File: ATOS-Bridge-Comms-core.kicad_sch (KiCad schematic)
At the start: 61 parts, among them J2 Conn_02x05_Counter_Clockwise, J3 Conn_01x09_Pin, Q1 2SC4617R, Q3 UMH3N, SW2 SKRPACE010, SW3 SKRPACE010, U1 LAN8720A-CP-TR, U2 AMS1117-3.3, U3 CH340C, U4 ESP32-WROOM-32UE, X1 ECS-2520MV-250-CN-TR

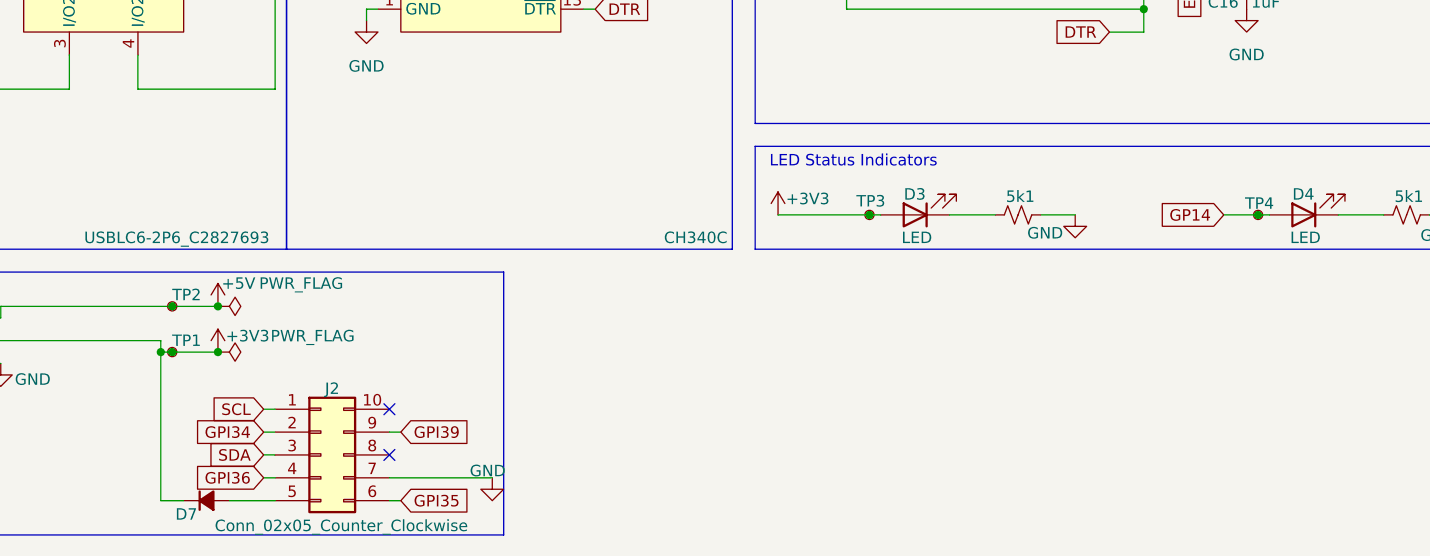
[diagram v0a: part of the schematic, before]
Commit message: Swap AMS1117-3.3 to LCSC C347222, add fab outputs
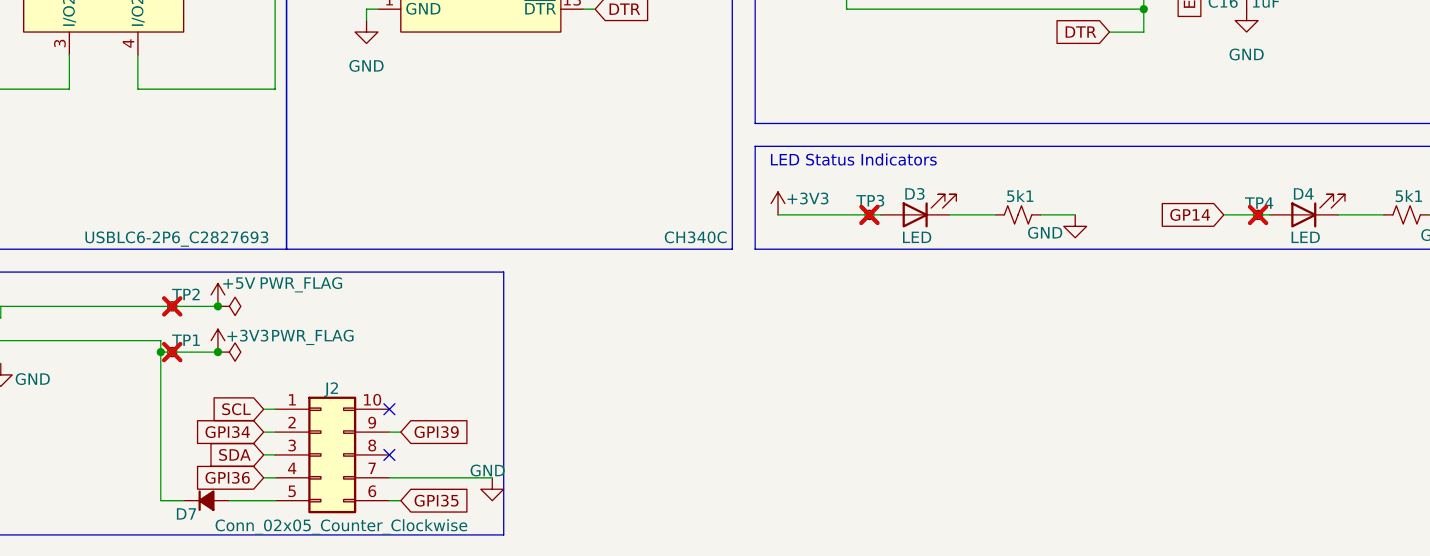
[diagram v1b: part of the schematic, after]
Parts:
- C1, C4, C5, C7, C9: LCSC Part (none) -> C19711
- C10: LCSC Part (none) -> C1556
- C12, C14, C2, C3, C6, C8: LCSC Part (none) -> C1525
- C15: LCSC Part (none) -> C86295
- C16: LCSC Part (none) -> C52923
- TP1, TP2, TP3, TP4: now not fitted
- U2: LCSC Part (none) -> C6186
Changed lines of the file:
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@@
 			)
 		)
+		(property "LCSC Part" "C6186"
+			(at 33.02 170.18 0)
+			(hide yes)
+			(show_name no)
+			(do_not_autoplace no)
+			(effects
+				(font
+					(size 1.27 1.27)
+				)
+			)
+		)
 		(pin "1"
 		)
@@
 			)
 		)
+		(property "LCSC Part" "C1525"
+			(at 102.87 118.11 90)
+			(hide yes)
+			(show_name no)
+			(do_not_autoplace no)
+			(effects
+				(font
+					(size 1.27 1.27)
+				)
+			)
+		)
 		(pin "2"
 		)
@@
 		(on_board yes)
 		(in_pos_files yes)
-		(dnp no)
+		(dnp yes)
 		(property "Reference" "TP4"
 			(at 259.588 158.75 90)
@@
 			)
 		)
+		(property "LCSC Part" "C1525"
+			(at 24.13 120.65 0)
+			(hide yes)
+			(show_name no)
+			(do_not_autoplace no)
+			(effects
+				(font
+					(size 1.27 1.27)
+				)
+			)
+		)
 		(pin "2"
 		)
@@
 			)
 		)
+		(property "LCSC Part" "C1525"
+			(at 88.9 29.21 0)
+			(hide yes)
+			(show_name no)
+			(do_not_autoplace no)
+			(effects
+				(font
+					(size 1.27 1.27)
+				)
+			)
+		)
 		(pin "2"
 		)
@@
 			)
 		)
+		(property "LCSC Part" "C1556"
+			(at 146.05 78.74 0)
+			(hide yes)
+			(show_name no)
+			(do_not_autoplace no)
+			(effects
+				(font
+					(size 1.27 1.27)
+				)
+			)
+		)
 		(pin "2"
 		)
@@
 			)
 		)
+		(property "LCSC Part" "C19711"
+			(at 100.33 29.21 0)
+			(hide yes)
+			(show_name no)
+			(do_not_autoplace no)
+			(effects
+				(font
+					(size 1.27 1.27)
+				)
+			)
+		)
 		(pin "2"
 		)
@@
 		(on_board yes)
 		(in_pos_files yes)
-		(dnp no)
+		(dnp yes)
 		(property "Reference" "TP1"
 			(at 137.16 173.99 0)
@@
 			)
 		)
+		(property "LCSC Part" "C1525"
+			(at 121.92 29.21 0)
+			(hide yes)
+			(show_name no)
+			(do_not_autoplace no)
+			(effects
+				(font
+					(size 1.27 1.27)
+				)
+			)
+		)
 		(pin "2"
 		)
@@
 			)
 		)
+		(property "LCSC Part" "C19711"
+			(at 19.05 31.75 0)
+			(hide yes)
+			(show_name no)
+			(do_not_autoplace no)
+			(effects
+				(font
+					(size 1.27 1.27)
+				)
+			)
+		)
 		(pin "2"
 		)
@@
 		(on_board yes)
 		(in_pos_files yes)
-		(dnp no)
+		(dnp yes)
 		(property "Reference" "TP3"
 			(at 216.408 158.496 90)
@@
 			)
 		)
+		(property "LCSC Part" "C1525"
+			(at 40.64 31.75 0)
+			(hide yes)
+			(show_name no)
+			(do_not_autoplace no)
+			(effects
+				(font
+					(size 1.27 1.27)
+				)
+			)
+		)
 		(pin "2"
 		)
@@
 			)
 		)
+		(property "LCSC Part" "C19711"
+			(at 133.35 29.21 0)
+			(hide yes)
+			(show_name no)
+			(do_not_autoplace no)
+			(effects
+				(font
+					(size 1.27 1.27)
+				)
+			)
+		)
 		(pin "2"
 		)
@@
 			)
 		)
+		(property "LCSC Part" "C1525"
+			(at 190.5 121.92 90)
+			(hide yes)
+			(show_name no)
+			(do_not_autoplace no)
+			(effects
+				(font
+					(size 1.27 1.27)
+				)
+			)
+		)
 		(pin "2"
 		)
@@
 			)
 		)
+		(property "LCSC Part" "C19711"
+			(at 102.87 110.49 90)
+			(hide yes)
+			(show_name no)
+			(do_not_autoplace no)
+			(effects
+				(font
+					(size 1.27 1.27)
+				)
+			)
+		)
 		(pin "2"
 		)
@@
 		(on_board yes)
 		(in_pos_files yes)
-		(dnp no)
+		(dnp yes)
 		(property "Reference" "TP2"
 			(at 137.16 168.91 0)
@@
 			)
 		)
+		(property "LCSC Part" "C86295"
+			(at 45.72 175.26 0)
+			(hide yes)
+			(show_name no)
+			(do_not_autoplace no)
+			(effects
+				(font
+					(size 1.27 1.27)
+				)
+			)
+		)
 		(pin "2"
 		)
@@
 			)
 		)
+		(property "LCSC Part" "C19711"
+			(at 17.78 175.26 0)
+			(hide yes)
+			(show_name no)
+			(do_not_autoplace no)
+			(effects
+				(font
+					(size 1.27 1.27)
+				)
+			)
+		)
 		(pin "2"
 		)
@@
 			(at 256.54 134.62 0)
 			(hide yes)
+			(show_name no)
+			(do_not_autoplace no)
+			(effects
+				(font
+					(size 1.27 1.27)
+				)
+			)
+		)
+		(property "LCSC Part" "C52923"
+			(at 256.54 134.62 0)
+			(hide yes)

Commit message: Post-design review interim changes
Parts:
- added H1, H2: M3, MountingHole:MountingHole_3.2mm_M3, symbol Mechanical:MountingHole
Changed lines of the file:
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@@
 	)
 	(rectangle
+		(start 55.88 166.37)
+		(end 97.79 195.58)
+		(stroke
+			(width 0)
+			(type default)
+		)
+		(fill
+			(type none)
+		)
+	)
+	(rectangle
 		(start 55.88 97.79)
 		(end 111.76 163.83)
@@
 	)
 	(symbol
+		(lib_id "Mechanical:MountingHole")
+		(at 63.5 186.69 0)
+		(unit 1)
+		(body_style 1)
+		(exclude_from_sim no)
+		(in_bom no)
+		(on_board yes)
+		(in_pos_files yes)
+		(dnp no)
+		(fields_autoplaced yes)
+		(property "Reference" "H2"
+			(at 66.04 185.4199 0)
+			(show_name no)
+			(do_not_autoplace no)
+			(effects
+				(font
+					(size 1.27 1.27)
+				)
+				(justify left)
+			)
+		)
+		(property "Value" "M3"
+			(at 66.04 187.9599 0)
+			(show_name no)
+			(do_not_autoplace no)
+			(effects
+				(font
+					(size 1.27 1.27)
+				)
+				(justify left)
+			)
+		)
+		(property "Footprint" "MountingHole:MountingHole_3.2mm_M3"
+			(at 63.5 186.69 0)
+			(hide yes)
+			(show_name no)
+			(do_not_autoplace no)
+			(effects
+				(font
+					(size 1.27 1.27)
+				)
+			)
+		)
+		(property "Datasheet" ""
+			(at 63.5 186.69 0)
+			(hide yes)
+			(show_name no)
+			(do_not_autoplace no)
+			(effects
+				(font
+					(size 1.27 1.27)
+				)
+			)
+		)
+		(property "Description" "Mounting Hole without connection"
+			(at 63.5 186.69 0)
+			(hide yes)
+			(show_name no)
+			(do_not_autoplace no)
+			(effects
+				(font
+					(size 1.27 1.27)
+				)
+			)
+		)
+		(instances
+			(project "ATOS-Bridge-Comms-core"
+				(path "/2b46a950-adb6-434b-928c-c069ab58e33e"
+					(reference "H2")
+					(unit 1)
+				)
+			)
+		)
+	)
+	(symbol
 		(lib_id "power:GND")
 		(at 100.33 31.75 0)
@@
 					(unit 1)
 				)
+			)
+		)
+	)
+	(symbol
+		(lib_id "Mechanical:MountingHole")
+		(at 63.5 179.07 0)
+		(unit 1)
+		(body_style 1)
+		(exclude_from_sim no)
+		(in_bom no)
+		(on_board yes)
+		(in_pos_files yes)
+		(dnp no)
+		(fields_autoplaced yes)
+		(property "Reference" "H1"
+			(at 66.04 177.7999 0)
+			(show_name no)
+			(do_not_autoplace no)
+			(effects
+				(font
+					(size 1.27 1.27)
+				)
+				(justify left)
+			)
+		)
+		(property "Value" "M3"
+			(at 66.04 180.3399 0)
+			(show_name no)
+			(do_not_autoplace no)
+			(effects
+				(font
+					(size 1.27 1.27)
+				)
+				(justify left)
+			)
+		)
+		(property "Footprint" "MountingHole:MountingHole_3.2mm_M3"
+			(at 63.5 179.07 0)
+			(hide yes)
+			(show_name no)
+			(do_not_autoplace no)
+			(effects
+				(font
+					(size 1.27 1.27)
+				)
+			)
+		)
+		(property "Datasheet" ""
+			(at 63.5 179.07 0)
+			(hide yes)
+			(show_name no)
+			(do_not_autoplace no)
+			(effects
+				(font
+					(size 1.27 1.27)
+				)
+			)
+		)
+		(property "Description" "Mounting Hole without connection"
+			(at 63.5 179.07 0)
+			(hide yes)
+			(show_name no)
+			(do_not_autoplace no)
+			(effects
+				(font
+					(size 1.27 1.27)
+				)
+			)
+		)
+		(instances
+			(project "ATOS-Bridge-Comms-core"
+				(path "/2b46a950-adb6-434b-928c-c069ab58e33e"
+					(reference "H1")
+					(unit 1)
+				)

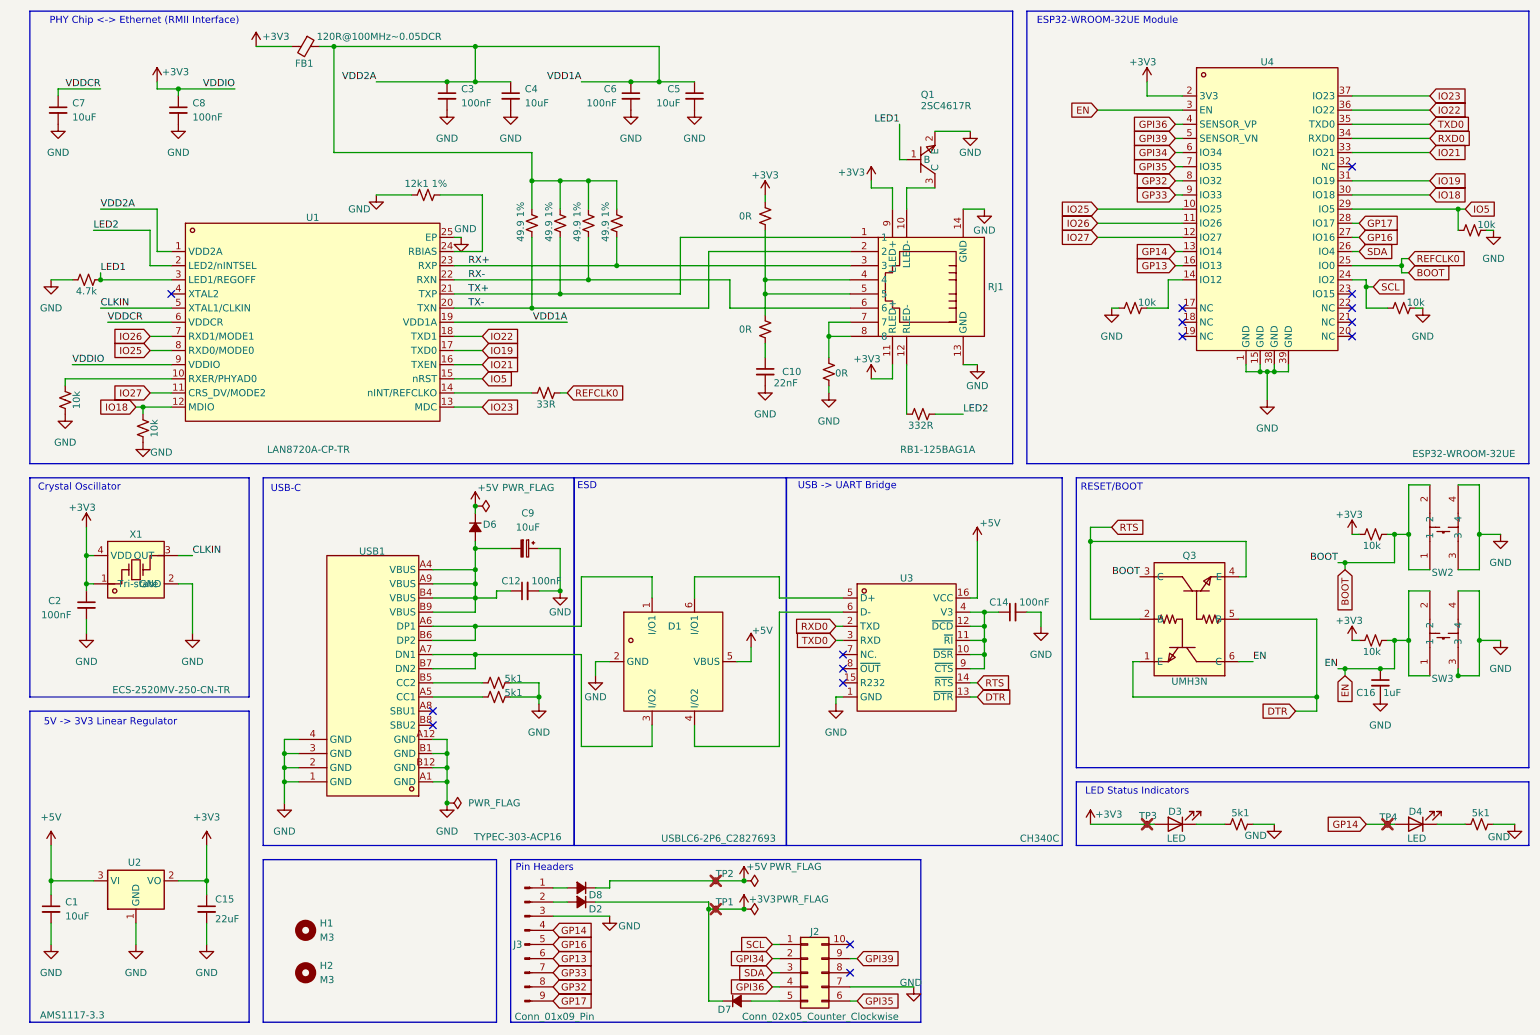
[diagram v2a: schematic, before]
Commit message: Cleaned up the board and fixed issues mentioned in DR-1
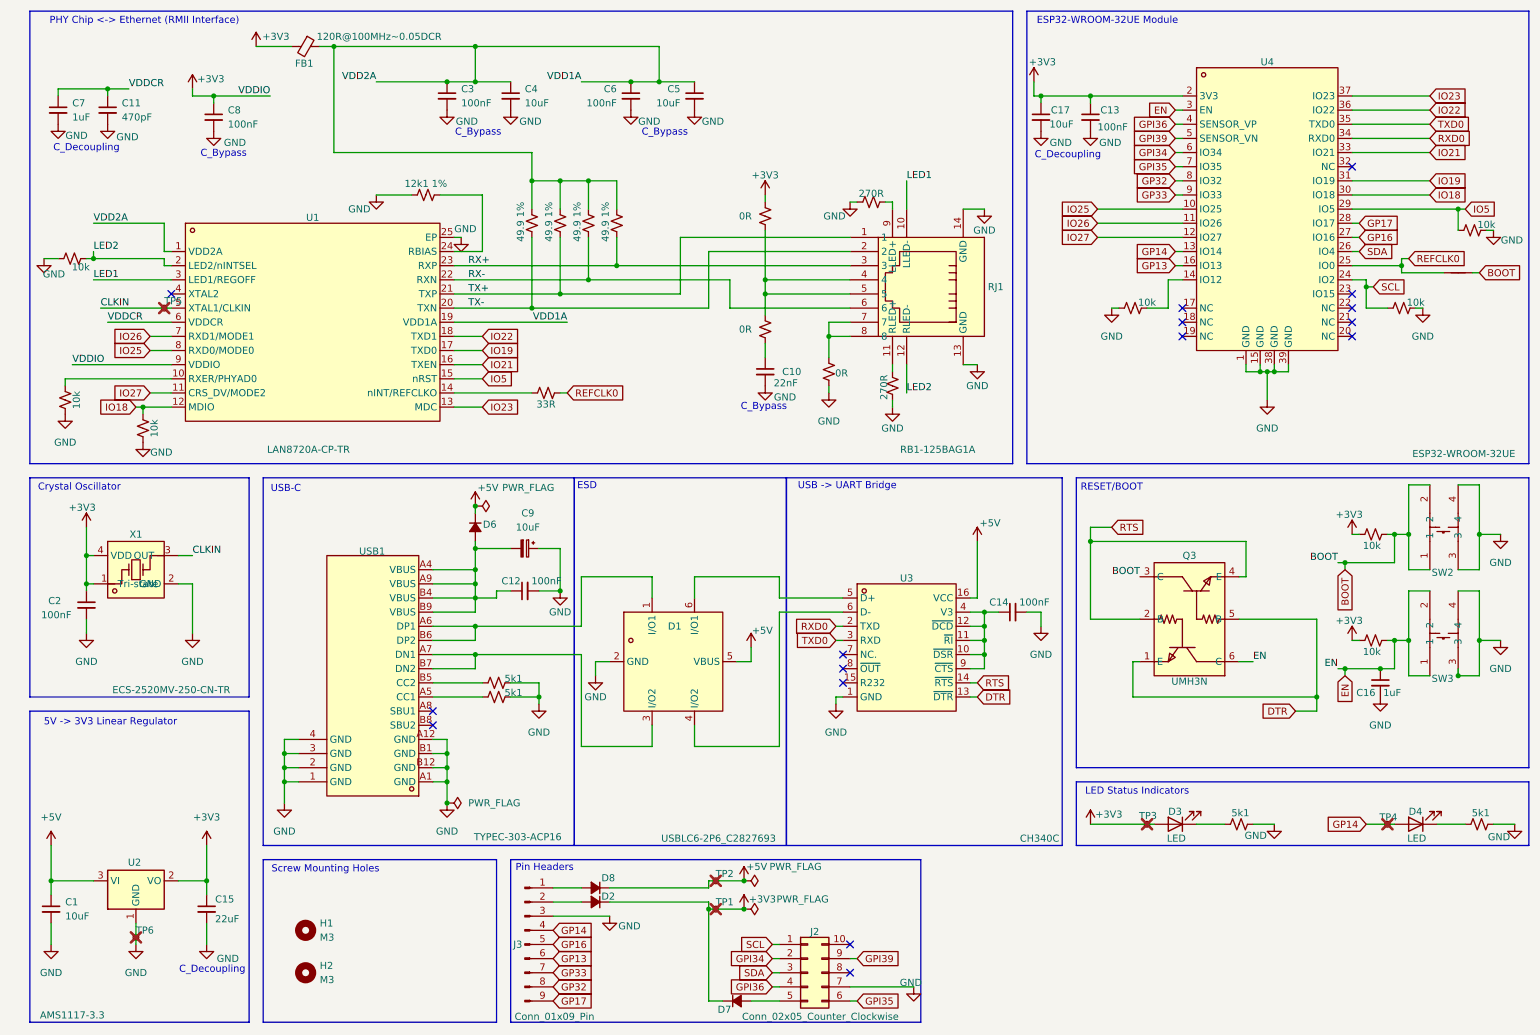
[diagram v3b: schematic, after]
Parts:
- removed Q1: 2SC4617R, imported-project-library:SOT-523-3_L1.6-W0.8-P1.00-LS1.6-BR, symbol imported-project-library:2SC4617R
- removed R1: 332R, Resistor_SMD:R_0402_1005Metric, symbol Device:R_Small_US
- removed R23: 4.7k, Resistor_SMD:R_0402_1005Metric, symbol Device:R_Small_US
- added C11: 470pF, Capacitor_SMD:C_0603_1608Metric, symbol Device:C_Small
- added C13: 100nF, Capacitor_SMD:C_0402_1005Metric, symbol Device:C_Small
- added C17: 10uF, Capacitor_SMD:C_0603_1608Metric, symbol Device:C_Small
- added NT1: NetTie_2, NetTie:NetTie-2_SMD_Pad0.5mm, symbol Device:NetTie_2
- added R24: 10k, Resistor_SMD:R_0402_1005Metric, symbol Device:R_Small_US
- added R25, R26: 270R, Resistor_SMD:R_0402_1005Metric, symbol Device:R_Small_US
- added TP5, TP6: TestPoint_Small, TestPoint:TestPoint_Pad_1.0x1.0mm, symbol Connector:TestPoint_Small
- C7: value 10uF -> 1uF
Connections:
- net +3V3: now also C13.1, C17.1; no longer RJ1.11 (RLED+), RJ1.9 (LLED+)
- net BOOT: now also NT1.2; no longer R4.1, U4.25 (IO0)
- net CLKIN: now also TP5.1
- net GND: now also C11.2, C13.2, C17.2, R24.1, R25.2, R26.2, TP6.1
- net LED1: now also RJ1.10 (LLED-)
- net LED2: now also RJ1.12 (RLED-), R24.2
- net VDDCR: now also C11.1
- new net: R26.1, RJ1.11 (RLED+)
- new net: R25.1, RJ1.9 (LLED+)
- new net REFCLK0: NT1.1, R4.1, U4.25 (IO0)
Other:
- note added: "C_Bypass"
- note added: "C_Decoupling"
- note added: "Screw Mounting Holes"
- moved on the sheet: C8, D2, D8
